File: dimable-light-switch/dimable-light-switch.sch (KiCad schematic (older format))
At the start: 17 parts

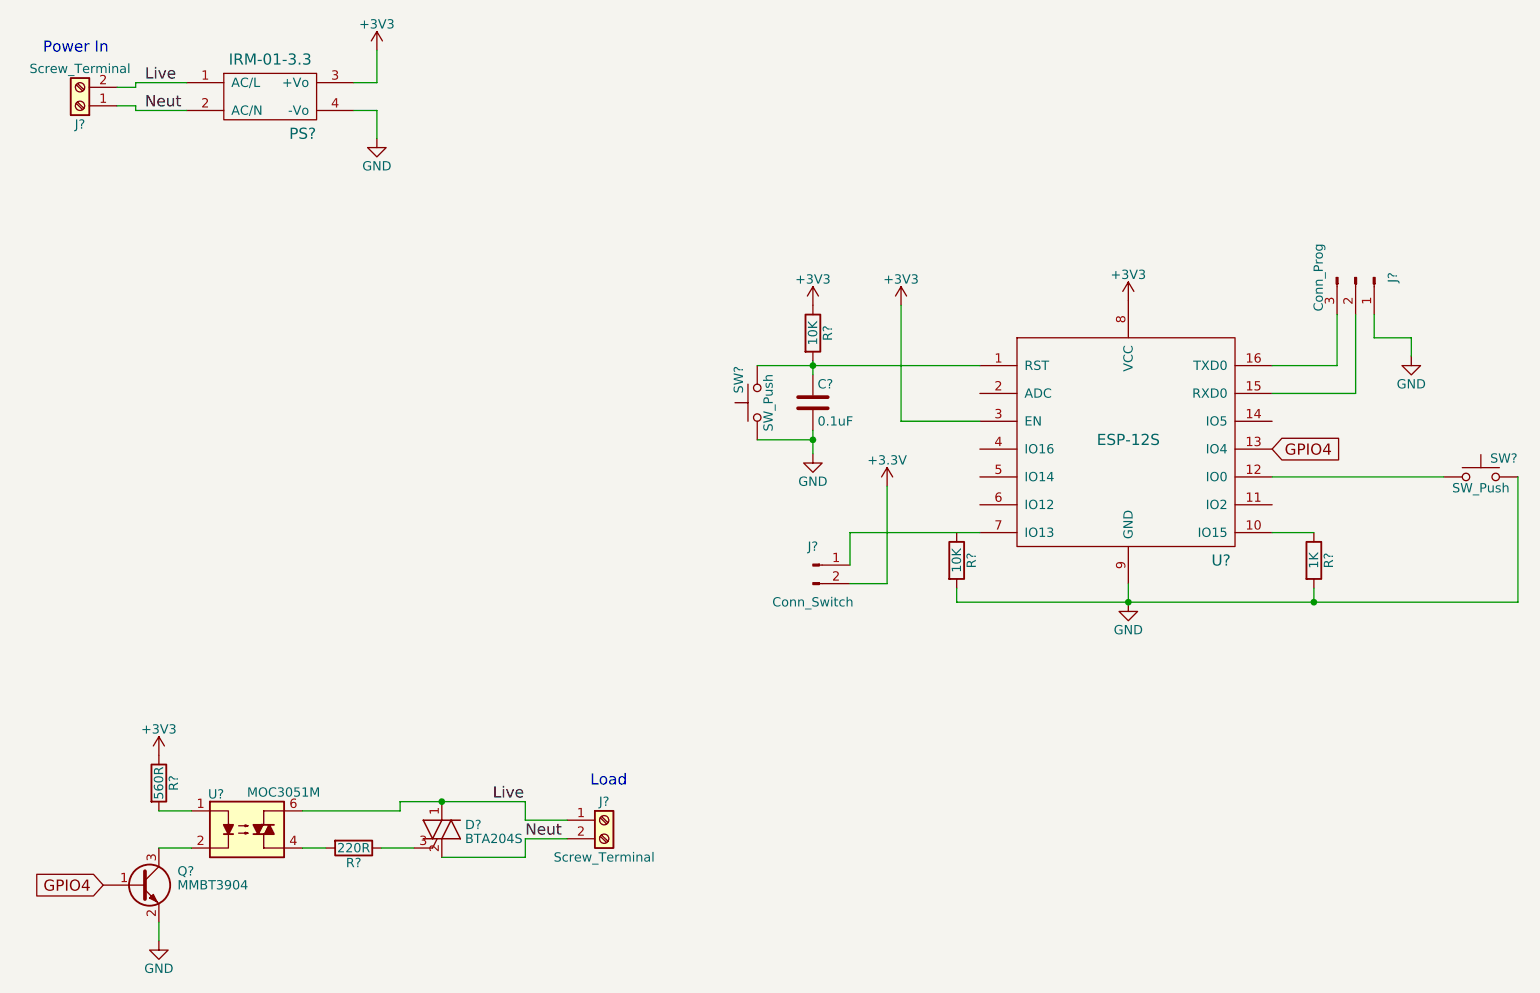
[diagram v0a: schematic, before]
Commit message: Assign/Create Footprints
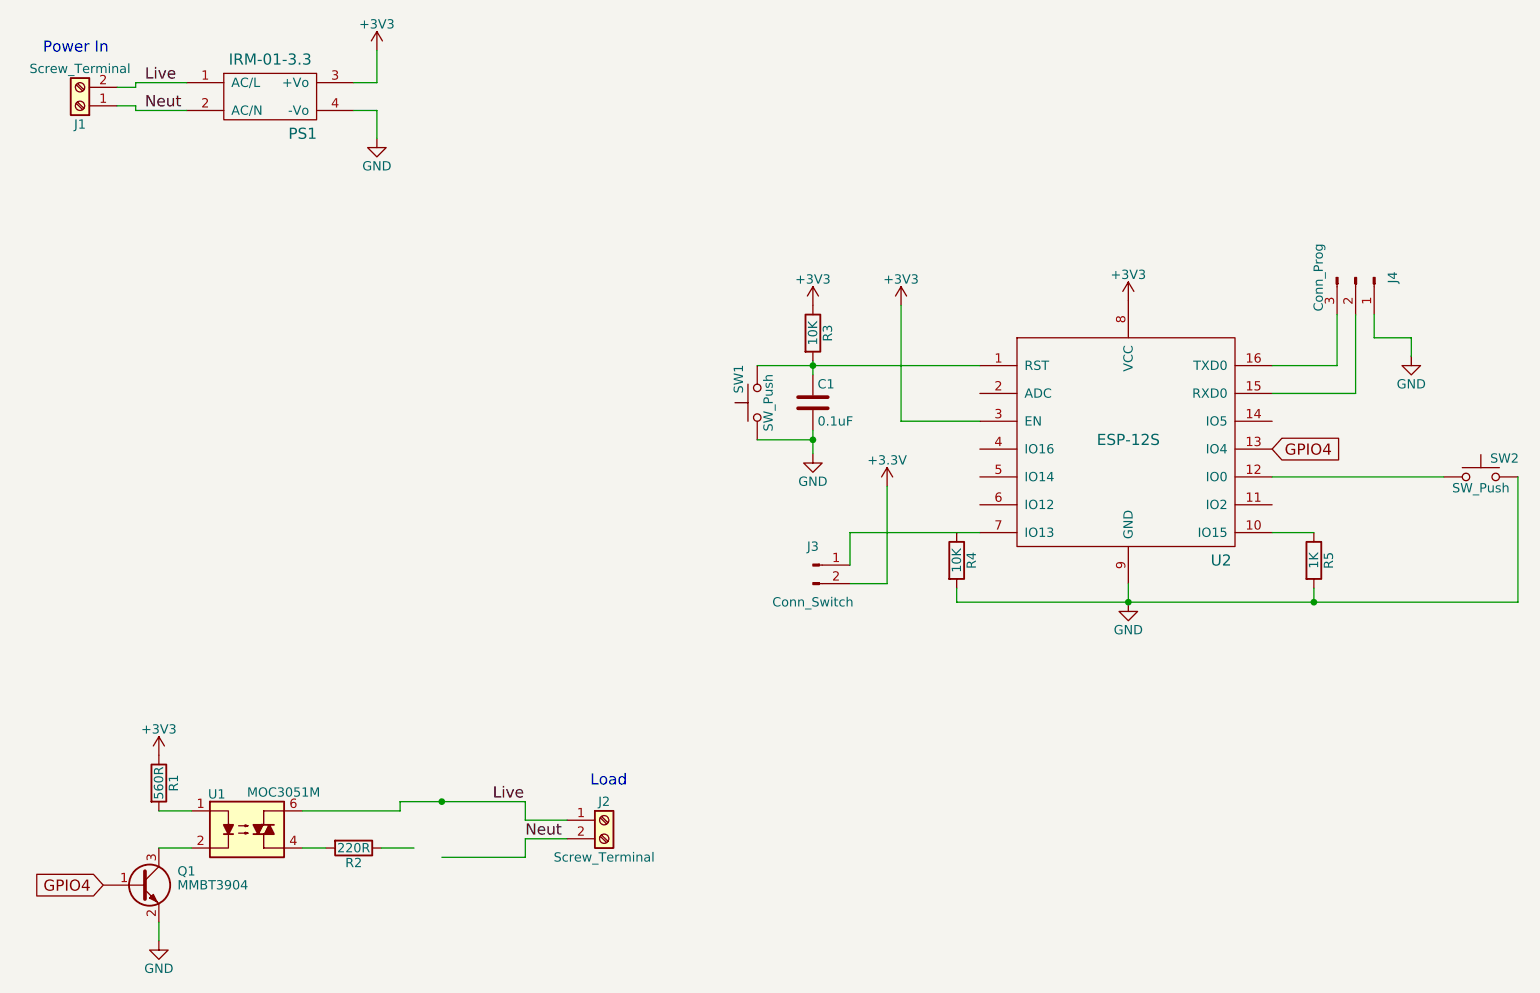
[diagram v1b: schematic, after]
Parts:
- removed D?: BTA204S, symbol Q_TRIAC_AAG
- C1: renamed from C?; footprint (none) -> Capacitors_SMD:C_1206_HandSoldering
- J3, J4: renamed from J?; footprint (none) -> Pin_Headers:Pin_Header_Straight_1x03_Pitch2.54mm
- R1, R2, R3, R4, R5: renamed from R?; footprint (none) -> Resistors_SMD:R_0805_HandSoldering
- SW1, SW2: renamed from SW?; footprint (none) -> Buttons_Switches_THT:SW_PUSH_6mm
- U1: renamed from U?; footprint (none) -> Housings_DIP:DIP-6_W7.62mm_SMDSocket_SmallPads
- U2: renamed from U?; footprint (none) -> ESP8266:ESP-12
- gave numbers to parts that had none: 4
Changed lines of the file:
@@
 $EndDescr
 $Comp
-L ESP-12S U?
+L ESP-12S U2
 U 1 1 5A9A23CB
 P 6850 3400
-F 0 "U?" H 7350 2800 60  0000 C CNN
+F 0 "U2" H 7350 2800 60  0000 C CNN
 F 1 "ESP-12S" H 6850 3450 60  0000 C CNN
-F 2 "" H 6350 3050 60  0001 C CNN
+F 2 "ESP8266:ESP-12" H 6350 3050 60  0001 C CNN
 F 3 "" H 6350 3050 60  0001 C CNN
 	1    6850 3400
@@
 $EndComp
 $Comp
-L +3V3 #PWR?
+L +3V3 #PWR01
 U 1 1 5A9A2442
 P 6850 2600
-F 0 "#PWR?" H 6850 2450 50  0001 C CNN
+F 0 "#PWR01" H 6850 2450 50  0001 C CNN
 F 1 "+3V3" H 6850 2740 50  0000 C CNN
 F 2 "" H 6850 2600 50  0001 C CNN
@@
 $EndComp
 $Comp
-L IRM-01-3.3 PS?
+L IRM-01-3.3 PS1
 U 1 1 5A9A2623
 P 2225 1500
-F 0 "PS?" H 2400 1300 60  0000 C CNN
+F 0 "PS1" H 2400 1300 60  0000 C CNN
 F 1 "IRM-01-3.3" H 2225 1700 60  0000 C CNN
 F 2 "" H 2075 1500 60  0001 C CNN
@@
 $EndComp
 $Comp
-L GND #PWR?
+L GND #PWR02
 U 1 1 5A9A27D2
 P 2800 1725
-F 0 "#PWR?" H 2800 1475 50  0001 C CNN
+F 0 "#PWR02" H 2800 1475 50  0001 C CNN
 F 1 "GND" H 2800 1575 50  0000 C CNN
 F 2 "" H 2800 1725 50  0001 C CNN
@@
 $EndComp
 $Comp
-L +3V3 #PWR?
+L +3V3 #PWR03
 U 1 1 5A9A2811
 P 2800 1250
-F 0 "#PWR?" H 2800 1100 50  0001 C CNN
+F 0 "#PWR03" H 2800 1100 50  0001 C CNN
 F 1 "+3V3" H 2800 1390 50  0000 C CNN
 F 2 "" H 2800 1250 50  0001 C CNN
@@
 $EndComp
 $Comp
-L Q_TRIAC_AAG D?
-U 1 1 5A9A30CA
-P 3150 5450
-F 0 "D?" H 3275 5475 50  0000 L CNN
-F 1 "BTA204S" H 3275 5400 50  0000 L CNN
-F 2 "" V 3225 5475 50  0001 C CNN
-F 3 "" V 3150 5450 50  0001 C CNN
-	1    3150 5450
-	1    0    0    -1
-$EndComp
-$Comp
-L Screw_Terminal_01x02 J?
+L Screw_Terminal_01x02 J2
 U 1 1 5A9A3C3B
 P 4025 5400
-F 0 "J?" H 4025 5500 50  0000 C CNN
+F 0 "J2" H 4025 5500 50  0000 C CNN
 F 1 "Screw_Terminal" H 4025 5200 50  0000 C CNN
 F 2 "" H 4025 5400 50  0001 C CNN
@@
 GPIO4
 $Comp
-L MOC3051M U?
+L MOC3051M U1
 U 1 1 5A9A56BA
 P 2100 5450
-F 0 "U?" H 1890 5640 50  0000 L CNN
+F 0 "U1" H 1890 5640 50  0000 L CNN
 F 1 "MOC3051M" H 2100 5650 50  0000 L CNN
-F 2 "" H 1900 5250 50  0001 L CIN
+F 2 "Housings_DIP:DIP-6_W7.62mm_SMDSocket_SmallPads" H 1900 5250 50  0001 L CIN
 F 3 "" H 2075 5450 50  0001 L CNN
 	1    2100 5450
@@
 $EndComp
 $Comp
-L R R?
+L R R1
 U 1 1 5A9A5843
 P 1625 5200
-F 0 "R?" V 1705 5200 50  0000 C CNN
+F 0 "R1" V 1705 5200 50  0000 C CNN
 F 1 "560R" V 1625 5200 50  0000 C CNN
-F 2 "" V 1555 5200 50  0001 C CNN
+F 2 "Resistors_SMD:R_0805_HandSoldering" V 1555 5200 50  0001 C CNN
 F 3 "" H 1625 5200 50  0001 C CNN
 	1    1625 5200
@@
 $EndComp
 $Comp
-L +3V3 #PWR?
+L +3V3 #PWR04
 U 1 1 5A9A5994
 P 1625 5050
-F 0 "#PWR?" H 1625 4900 50  0001 C CNN
+F 0 "#PWR04" H 1625 4900 50  0001 C CNN
 F 1 "+3V3" H 1625 5190 50  0000 C CNN
 F 2 "" H 1625 5050 50  0001 C CNN
@@
 $EndComp
 $Comp
-L MMBT3904 Q?
+L MMBT3904 Q1
 U 1 1 5A9A5A51
 P 1525 5750
-F 0 "Q?" H 1725 5825 50  0000 L CNN
+F 0 "Q1" H 1725 5825 50  0000 L CNN
 F 1 "MMBT3904" H 1725 5750 50  0000 L CNN
 F 2 "TO_SOT_Packages_SMD:SOT-23" H 1725 5675 50  0001 L CIN
@@
 GPIO4
 $Comp
-L GND #PWR?
+L GND #PWR05
 U 1 1 5A9A5B6B
 P 1625 6050
-F 0 "#PWR?" H 1625 5800 50  0001 C CNN
+F 0 "#PWR05" H 1625 5800 50  0001 C CNN
 F 1 "GND" H 1625 5900 50  0000 C CNN
 F 2 "" H 1625 6050 50  0001 C CNN
@@
 $EndComp
 $Comp
-L R R?
+L R R2
 U 1 1 5A9A5B9F
 P 2675 5550
-F 0 "R?" V 2755 5550 50  0000 C CNN
+F 0 "R2" V 2755 5550 50  0000 C CNN
 F 1 "220R" V 2675 5550 50  0000 C CNN
-F 2 "" V 2605 5550 50  0001 C CNN
+F 2 "Resistors_SMD:R_0805_HandSoldering" V 2605 5550 50  0001 C CNN
 F 3 "" H 2675 5550 50  0001 C CNN
 	1    2675 5550
@@
 $EndComp
 $Comp
-L R R?
+L R R3
 U 1 1 5A9A60A7
 P 5150 2775
-F 0 "R?" V 5230 2775 50  0000 C CNN
+F 0 "R3" V 5230 2775 50  0000 C CNN
 F 1 "10K" V 5150 2775 50  0000 C CNN
-F 2 "" V 5080 2775 50  0001 C CNN
+F 2 "Resistors_SMD:R_0805_HandSoldering" V 5080 2775 50  0001 C CNN
 F 3 "" H 5150 2775 50  0001 C CNN
 	1    5150 2775
@@
 $EndComp
 $Comp
-L +3V3 #PWR?
+L +3V3 #PWR06
 U 1 1 5A9A6197
 P 5150 2625
-F 0 "#PWR?" H 5150 2475 50  0001 C CNN
+F 0 "#PWR06" H 5150 2475 50  0001 C CNN
 F 1 "+3V3" H 5150 2765 50  0000 C CNN
 F 2 "" H 5150 2625 50  0001 C CNN
@@
 $EndComp
 $Comp
-L SW_Push SW?
+L SW_Push SW2
 U 1 1 5A9A61E3
 P 8750 3550
-F 0 "SW?" H 8800 3650 50  0000 L CNN
+F 0 "SW2" H 8800 3650 50  0000 L CNN
 F 1 "SW_Push" H 8750 3490 50  0000 C CNN
-F 2 "" H 8750 3750 50  0001 C CNN
+F 2 "Buttons_Switches_THT:SW_PUSH_6mm" H 8750 3750 50  0001 C CNN
 F 3 "" H 8750 3750 50  0001 C CNN
 	1    8750 3550
@@
 $EndComp
 $Comp
-L SW_Push SW?
+L SW_Push SW1
 U 1 1 5A9A6392
 P 4850 3150
-F 0 "SW?" H 4900 3250 50  0000 L CNN
+F 0 "SW1" H 4900 3250 50  0000 L CNN
 F 1 "SW_Push" H 4850 3090 50  0000 C CNN
-F 2 "" H 4850 3350 50  0001 C CNN
+F 2 "Buttons_Switches_THT:SW_PUSH_6mm" H 4850 3350 50  0001 C CNN
 F 3 "" H 4850 3350 50  0001 C CNN
 	1    4850 3150
@@
 $EndComp
 $Comp
-L C C?
+L C C1
 U 1 1 5A9A6507
 P 5150 3150
-F 0 "C?" H 5175 3250 50  0000 L CNN
+F 0 "C1" H 5175 3250 50  0000 L CNN
 F 1 "0.1uF" H 5175 3050 50  0000 L CNN
-F 2 "" H 5188 3000 50  0001 C CNN
+F 2 "Capacitors_SMD:C_1206_HandSoldering" H 5188 3000 50  0001 C CNN
 F 3 "" H 5150 3150 50  0001 C CNN
 	1    5150 3150
@@
 $EndComp
 $Comp
-L GND #PWR?
+L GND #PWR07
 U 1 1 5A9A65DC
 P 5150 3425
-F 0 "#PWR?" H 5150 3175 50  0001 C CNN
+F 0 "#PWR07" H 5150 3175 50  0001 C CNN
 F 1 "GND" H 5150 3275 50  0000 C CNN
 F 2 "" H 5150 3425 50  0001 C CNN
@@
 $EndComp
 $Comp
-L +3V3 #PWR?
+L +3V3 #PWR08
 U 1 1 5A9A6612
 P 5625 2625
-F 0 "#PWR?" H 5625 2475 50  0001 C CNN
+F 0 "#PWR08" H 5625 2475 50  0001 C CNN
 F 1 "+3V3" H 5625 2765 50  0000 C CNN
 F 2 "" H 5625 2625 50  0001 C CNN
@@
 $EndComp
 $Comp
-L R R?
+L R R5
 U 1 1 5A9A6DB4
 P 7850 4000
-F 0 "R?" V 7930 4000 50  0000 C CNN
+F 0 "R5" V 7930 4000 50  0000 C CNN
 F 1 "1K" V 7850 4000 50  0000 C CNN
-F 2 "" V 7780 4000 50  0001 C CNN
+F 2 "Resistors_SMD:R_0805_HandSoldering" V 7780 4000 50  0001 C CNN
 F 3 "" H 7850 4000 50  0001 C CNN
 	1    7850 4000
@@
 $EndComp
 $Comp
-L GND #PWR?
+L GND #PWR09
 U 1 1 5A9A6ED7
 P 6850 4225
-F 0 "#PWR?" H 6850 3975 50  0001 C CNN
+F 0 "#PWR09" H 6850 3975 50  0001 C CNN
 F 1 "GND" H 6850 4075 50  0000 C CNN
 F 2 "" H 6850 4225 50  0001 C CNN
@@
 $EndComp
 $Comp
-L Screw_Terminal_01x02 J?
+L Screw_Terminal_01x02 J1
 U 1 1 5A9A7222
 P 1200 1550
-F 0 "J?" H 1200 1650 50  0000 C CNN
+F 0 "J1" H 1200 1650 50  0000 C CNN
 F 1 "Screw_Terminal" H 1200 1350 50  0000 C CNN
 F 2 "" H 1200 1550 50  0001 C CNN
@@
 	8375 2800 8375 2900
 $Comp
-L GND #PWR?
+L GND #PWR010
 U 1 1 5A9A8871
 P 8375 2900
-F 0 "#PWR?" H 8375 2650 50  0001 C CNN
+F 0 "#PWR010" H 8375 2650 50  0001 C CNN
 F 1 "GND" H 8375 2750 50  0000 C CNN
 F 2 "" H 8375 2900 50  0001 C CNN
@@
 $EndComp
 $Comp
-L Conn_01x02_Male J?
+L Conn_01x02_Male J3
 U 1 1 5A9ACD69
 P 5150 4025
-F 0 "J?" H 5150 4125 50  0000 C CNN
+F 0 "J3" H 5150 4125 50  0000 C CNN
 F 1 "Conn_Switch" H 5150 3825 50  0000 C CNN
-F 2 "" H 5150 4025 50  0001 C CNN
+F 2 "Pin_Headers:Pin_Header_Straight_1x03_Pitch2.54mm" H 5150 4025 50  0001 C CNN
 F 3 "" H 5150 4025 50  0001 C CNN
 	1    5150 4025
@@
 $EndComp
 $Comp
-L Conn_01x03_Male J?
+L Conn_01x03_Male J4
 U 1 1 5A9ACE3A
 P 8075 2475
-F 0 "J?" H 8075 2675 50  0000 C CNN
+F 0 "J4" H 8075 2675 50  0000 C CNN
 F 1 "Conn_Prog" H 8075 2275 50  0000 C CNN
-F 2 "" H 8075 2475 50  0001 C CNN
+F 2 "Pin_Headers:Pin_Header_Straight_1x03_Pitch2.54mm" H 8075 2475 50  0001 C CNN
 F 3 "" H 8075 2475 50  0001 C CNN
 	1    8075 2475
@@
 	5350 3850 5350 4025
 $Comp
-L R R?
+L R R4
 U 1 1 5A9AD1CA
 P 5925 4000
-F 0 "R?" V 6005 4000 50  0000 C CNN
+F 0 "R4" V 6005 4000 50  0000 C CNN
 F 1 "10K" V 5925 4000 50  0000 C CNN
-F 2 "" V 5855 4000 50  0001 C CNN
+F 2 "Resistors_SMD:R_0805_HandSoldering" V 5855 4000 50  0001 C CNN
 F 3 "" H 5925 4000 50  0001 C CNN
 	1    5925 4000
@@
 Connection ~ 6850 4225
 $Comp
-L +3.3V #PWR?
+L +3.3V #PWR011
 U 1 1 5A9AD3ED
 P 5550 3600
-F 0 "#PWR?" H 5550 3450 50  0001 C CNN
+F 0 "#PWR011" H 5550 3450 50  0001 C CNN
 F 1 "+3.3V" H 5550 3740 50  0000 C CNN
 F 2 "" H 5550 3600 50  0001 C CNN

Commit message: PCB Routing
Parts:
- added D1: BTA204S, SOT428:SOT428, symbol BTA204S
- J1, J2: footprint (none) -> TerminalBlocks_Phoenix:TerminalBlock_Phoenix_PT-3.5mm_2pol
- PS1: footprint (none) -> SOT428:IRM-01-3.3
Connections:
- net labels removed: Live, Neut
- wire segments 47 -> 45
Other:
- note added: "1935161"
- moved on the sheet: J1
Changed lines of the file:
@@
-$EndComp
-$Comp
-L IRM-01-3.3 PS1
-U 1 1 5A9A2623
-P 2225 1500
-F 0 "PS1" H 2400 1300 60  0000 C CNN
-F 1 "IRM-01-3.3" H 2225 1700 60  0000 C CNN
-F 2 "" H 2075 1500 60  0001 C CNN
-F 3 "" H 2075 1500 60  0001 C CNN
-	1    2225 1500
-	1    0    0    -1
 $EndComp
 $Comp
@@
 F 0 "J2" H 4025 5500 50  0000 C CNN
 F 1 "Screw_Terminal" H 4025 5200 50  0000 C CNN
-F 2 "" H 4025 5400 50  0001 C CNN
+F 2 "TerminalBlocks_Phoenix:TerminalBlock_Phoenix_PT-3.5mm_2pol" H 4025 5400 50  0001 C CNN
 F 3 "" H 4025 5400 50  0001 C CNN
 	1    4025 5400
@@
 L Screw_Terminal_01x02 J1
 U 1 1 5A9A7222
-P 1200 1550
-F 0 "J1" H 1200 1650 50  0000 C CNN
-F 1 "Screw_Terminal" H 1200 1350 50  0000 C CNN
-F 2 "" H 1200 1550 50  0001 C CNN
-F 3 "" H 1200 1550 50  0001 C CNN
-	1    1200 1550
-	-1   0    0    1
-$EndComp
-Text Label 1550 1425 0    60   ~ 0
-Live
-Text Label 1550 1575 0    60   ~ 0
-Neut
-Text Label 3600 5500 0    60   ~ 0
-Neut
-Text Label 3425 5300 0    60   ~ 0
-Live
+P 1575 1850
+F 0 "J1" H 1575 1950 50  0000 C CNN
+F 1 "Screw_Terminal" H 1575 1650 50  0000 C CNN
+F 2 "TerminalBlocks_Phoenix:TerminalBlock_Phoenix_PT-3.5mm_2pol" H 1575 1850 50  0001 C CNN
+F 3 "" H 1575 1850 50  0001 C CNN
+	1    1575 1850
+	0    1    1    0
+$EndComp
 Text Notes 3950 5225 0    60   ~ 0
 Load
@@
 	7850 4150 7850 4225
 Connection ~ 7850 4225
-Wire Wire Line
-	1400 1450 1500 1450
-Wire Wire Line
-	1500 1450 1500 1425
-Wire Wire Line
-	1500 1425 1775 1425
-Wire Wire Line
-	1775 1575 1500 1575
-Wire Wire Line
-	1500 1575 1500 1550
-Wire Wire Line
-	1500 1550 1400 1550
 Wire Wire Line
 	7625 2950 7975 2950
@@
 Wire Wire Line
 	5550 4125 5550 3600
+$Comp
+L BTA204S D1
+U 1 1 5A9AEBB1
+P 3150 5450
+F 0 "D1" H 3275 5475 50  0000 L CNN
+F 1 "BTA204S" H 3275 5400 50  0000 L CNN
+F 2 "SOT428:SOT428" V 3225 5475 50  0001 C CNN
+F 3 "" V 3150 5450 50  0001 C CNN
+	1    3150 5450
+	1    0    0    -1
+$EndComp
+$Comp
+L IRM-01-3.3 PS1
+U 1 1 5A9AF049
+P 2225 1500
+F 0 "PS1" H 2400 1300 60  0000 C CNN
+F 1 "IRM-01-3.3" H 2225 1700 60  0000 C CNN
+F 2 "SOT428:IRM-01-3.3" H 2075 1500 60  0001 C CNN
+F 3 "" H 2075 1500 60  0001 C CNN
+	1    2225 1500
+	1    0    0    -1
+$EndComp
+Text Notes 3850 5725 0    60   ~ 0
+1935161
+Wire Wire Line
+	1775 1575 1475 1575
+Wire Wire Line
+	1475 1575 1475 1650
+Wire Wire Line
+	1775 1425 1575 1425
+Wire Wire Line
+	1575 1425 1575 1650
 $EndSCHEMATC
